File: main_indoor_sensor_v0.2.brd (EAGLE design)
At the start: 15 parts

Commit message: Added Gerber file...
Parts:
- moved R4 1.27 mm to (22.9, 44.5)
- moved U$2 1.27 mm to (49.5, 40.6)
- moved U$6 1.27 mm to (11.4, 40.6)
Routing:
- net N$19: track 5.66 -> 3.94 mm
- net N$8: track 19.0 -> 17.8 mm
- net N$16: track 19.8 -> 18.5 mm
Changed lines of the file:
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@@
 <board>
 <plain>
-<hole x="2.54" y="48.26" drill="3.048"/>
-<hole x="71.12" y="48.26" drill="3.048"/>
+<hole x="2.54" y="46.99" drill="3.048"/>
+<hole x="71.12" y="46.99" drill="3.048"/>
 <hole x="2.54" y="2.54" drill="3.048"/>
 <hole x="71.12" y="2.54" drill="3.048"/>
@@
 <elements>
 <element name="U$3" library="piweather" package="DHT22" value="DHT22WHITE" x="64.77" y="45.72" rot="R90"/>
-<element name="U$6" library="piweather" package="RGB_LED" value="RGB_LED5MM" x="11.43" y="41.91"/>
+<element name="U$6" library="piweather" package="RGB_LED" value="RGB_LED5MM" x="11.43" y="40.64"/>
 <element name="P_IN" library="piweather" package="2PINCONNECTOR" value="2PINCONNECTORSIMPLE" x="25.4" y="12.7" rot="R180"/>
 <element name="R1" library="eagle-ltspice" package="0204/7" value="" x="48.26" y="27.94" rot="R90">
@@
 <attribute name="SPICEPREFIX" value="R" x="22.86" y="40.64" size="1.778" layer="27" display="off"/>
 </element>
-<element name="R4" library="eagle-ltspice" package="0204/7" value="" x="22.86" y="45.72">
-<attribute name="SPICEMODEL" value="NONE" x="22.86" y="45.72" size="1.778" layer="27" display="off"/>
-<attribute name="SPICEPREFIX" value="R" x="22.86" y="45.72" size="1.778" layer="27" display="off"/>
+<element name="R4" library="eagle-ltspice" package="0204/7" value="" x="22.86" y="44.45">
+<attribute name="SPICEMODEL" value="NONE" x="22.86" y="44.45" size="1.778" layer="27" display="off"/>
+<attribute name="SPICEPREFIX" value="R" x="22.86" y="44.45" size="1.778" layer="27" display="off"/>
 </element>
 <element name="NCP1402" library="piweather" package="NCP1402" value="NCP1402SPARKFUN" x="17.78" y="9.525" rot="R180"/>
@@
 <element name="VIN2" library="pinhead" package="1X01" value="" x="24.13" y="3.81"/>
 <element name="U$1" library="piweather" package="ATMEGA328P" value="ATMEGA328PARDUINO" x="35.56" y="27.94"/>
-<element name="U$2" library="piweather" package="KRS0612_RIGHT" value="KRS_0612_OK" x="49.53" y="41.91" rot="R90"/>
+<element name="U$2" library="piweather" package="KRS0612_RIGHT" value="KRS_0612_OK" x="49.53" y="40.64" rot="R90"/>
 </elements>
 <signals>
@@
 <contactref element="R4" pad="2"/>
 <contactref element="U$1" pad="3"/>
-<wire x1="26.67" y1="45.72" x2="29.21" y2="45.72" width="0.4064" layer="16"/>
-<wire x1="29.21" y1="45.72" x2="29.21" y2="31.75" width="0.4064" layer="16"/>
+<wire x1="26.67" y1="44.45" x2="29.21" y2="44.45" width="0.4064" layer="16"/>
+<wire x1="29.21" y1="44.45" x2="29.21" y2="31.75" width="0.4064" layer="16"/>
 <wire x1="29.21" y1="31.75" x2="31.75" y2="31.75" width="0.4064" layer="16"/>
 </signal>
@@
 <contactref element="U$6" pad="BLUE"/>
 <contactref element="R2" pad="1"/>
-<wire x1="11.43" y1="38.1" x2="19.05" y2="36.83" width="0.4064" layer="16"/>
+<wire x1="11.43" y1="36.83" x2="19.05" y2="36.83" width="0.4064" layer="16"/>
 </signal>
 <signal name="N$10">
 <contactref element="U$6" pad="GREEN"/>
 <contactref element="R3" pad="1"/>
-<wire x1="11.43" y1="40.64" x2="19.05" y2="40.64" width="0.4064" layer="16"/>
+<wire x1="11.43" y1="39.37" x2="19.05" y2="40.64" width="0.4064" layer="16"/>
 </signal>
 <signal name="N$11">
@@
 <contactref element="U$6" pad="RED"/>
 <contactref element="R4" pad="1"/>
-<wire x1="11.43" y1="45.72" x2="19.05" y2="45.72" width="0.4064" layer="16"/>
+<wire x1="11.43" y1="44.45" x2="19.05" y2="44.45" width="0.4064" layer="16"/>
 </signal>
 <signal name="N$15">
@@
 <vertex x="0" y="0"/>
 <vertex x="73.66" y="0"/>
-<vertex x="73.66" y="50.8"/>
-<vertex x="0" y="50.8"/>
+<vertex x="73.66" y="49.53"/>
+<vertex x="0" y="49.53"/>
 </polygon>
 <contactref element="GY-65" pad="GND"/>
@@
 <wire x1="31.75" y1="46.99" x2="43.18" y2="46.99" width="0.4064" layer="16"/>
 <contactref element="U$2" pad="1"/>
-<wire x1="45.03" y1="48.41" x2="43.18" y2="48.41" width="0.4064" layer="16"/>
-<wire x1="43.18" y1="48.41" x2="43.18" y2="46.99" width="0.4064" layer="16"/>
+<wire x1="45.03" y1="47.14" x2="43.18" y2="47.14" width="0.4064" layer="16"/>
+<wire x1="43.18" y1="47.14" x2="43.18" y2="46.99" width="0.4064" layer="16"/>
 </signal>
 <signal name="N$17">
@@
 <contactref element="R5" pad="1"/>
 <contactref element="U$2" pad="VCC"/>
-<wire x1="45.03" y1="41.91" x2="44.45" y2="41.91" width="0.4064" layer="16"/>
-<wire x1="44.45" y1="41.91" x2="44.45" y2="36.83" width="0.4064" layer="16"/>
+<wire x1="45.03" y1="40.64" x2="44.45" y2="39.37" width="0.4064" layer="16"/>
+<wire x1="44.45" y1="39.37" x2="44.45" y2="36.83" width="0.4064" layer="16"/>
 </signal>
 <signal name="N$14">

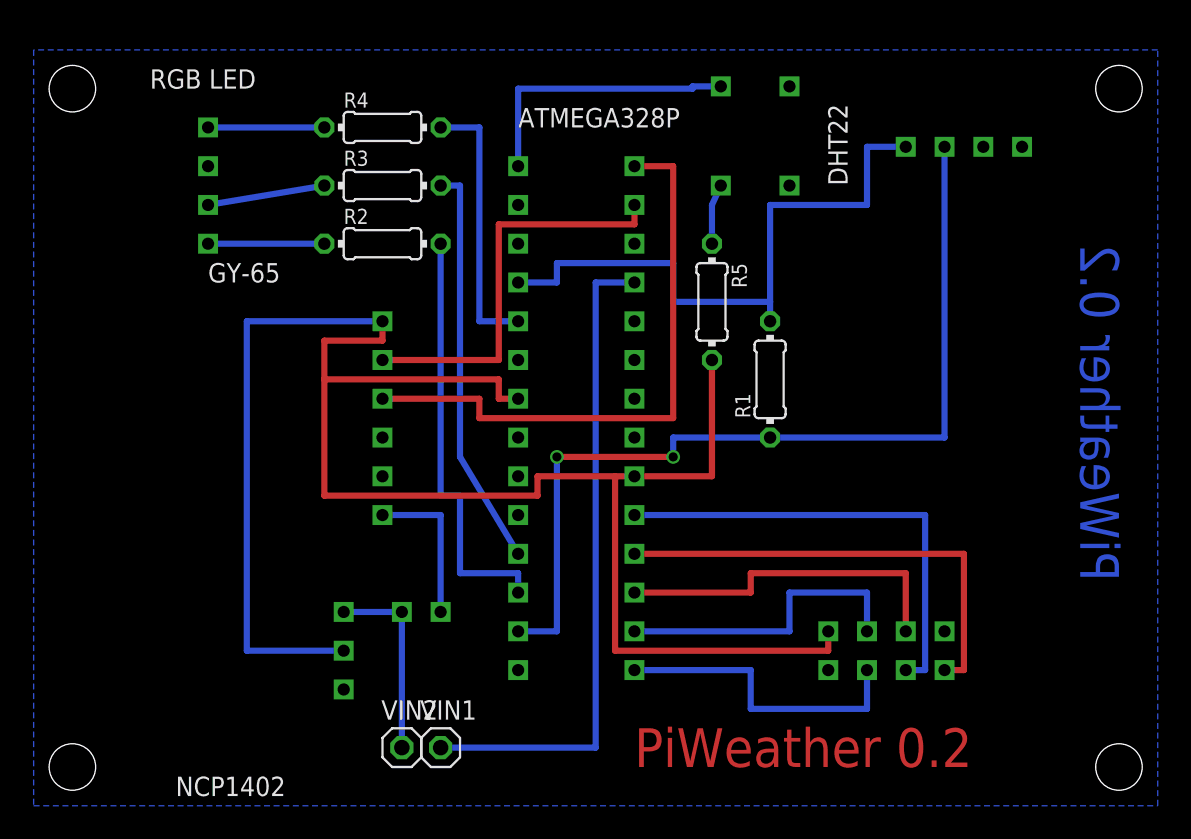
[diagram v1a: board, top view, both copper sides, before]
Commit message: Nouvelle version avec la board outline :o
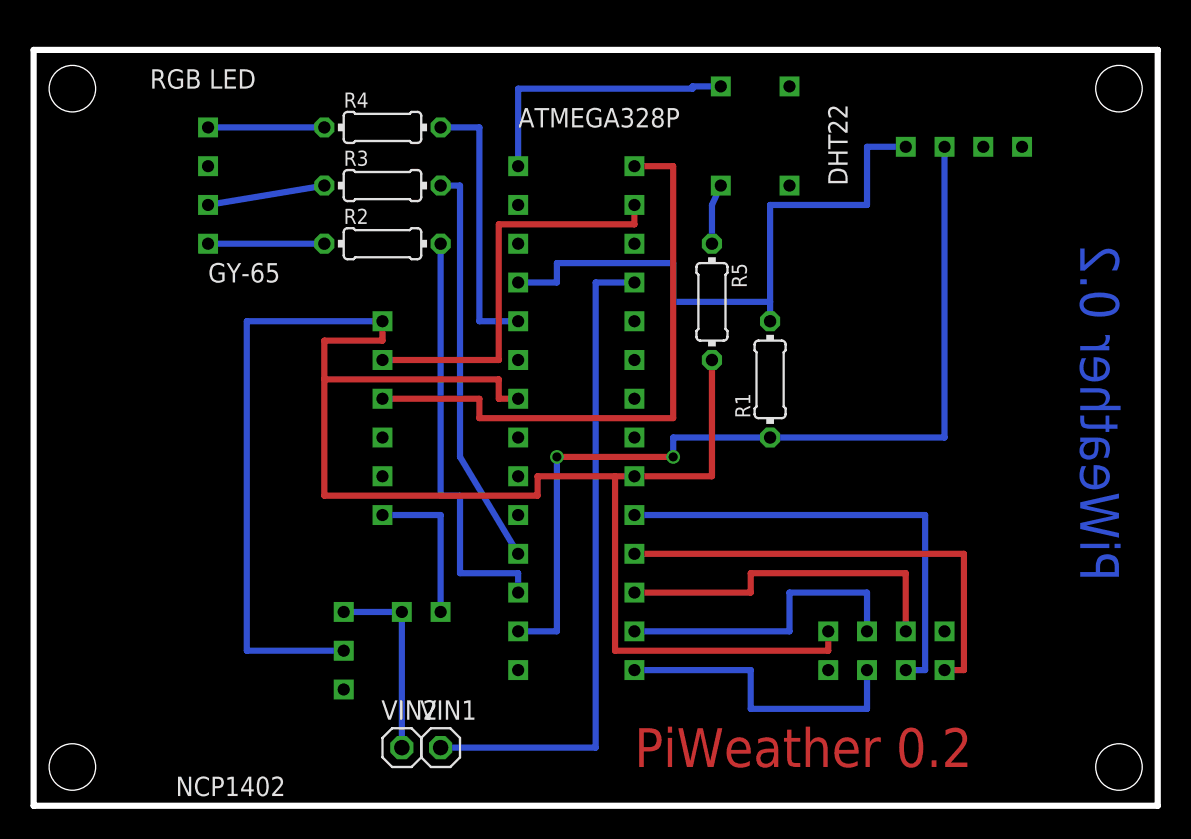
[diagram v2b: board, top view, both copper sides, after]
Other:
- board outline added: 73.7 x 49.5 mm
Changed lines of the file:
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@@
 <layer number="18" name="Vias" color="2" fill="1" visible="yes" active="yes"/>
 <layer number="19" name="Unrouted" color="6" fill="1" visible="yes" active="yes"/>
-<layer number="20" name="Dimension" color="15" fill="1" visible="yes" active="yes"/>
+<layer number="20" name="Dimension" color="10" fill="1" visible="yes" active="yes"/>
 <layer number="21" name="tPlace" color="7" fill="1" visible="yes" active="yes"/>
 <layer number="22" name="bPlace" color="7" fill="1" visible="yes" active="yes"/>
@@
 <text x="39.37" y="2.54" size="2.54" layer="1">PiWeather 0.2</text>
 <text x="71.12" y="36.83" size="2.54" layer="16" rot="MR270">PiWeather 0.2</text>
+<wire x1="0" y1="49.53" x2="73.66" y2="49.53" width="0.4064" layer="20"/>
+<wire x1="73.66" y1="49.53" x2="73.66" y2="0" width="0.4064" layer="20"/>
+<wire x1="73.66" y1="0" x2="0" y2="0" width="0.4064" layer="20"/>
+<wire x1="0" y1="0" x2="0" y2="49.53" width="0.4064" layer="20"/>
 </plain>
 <attributes>
